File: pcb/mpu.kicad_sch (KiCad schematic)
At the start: 27 parts, among them J13 Conn_01x04, U2 STM32U585CIUxQ, Y1 ECS-160-8-36B2-CKM-TR, Y2 CM7V-T1A-32.768KHZ

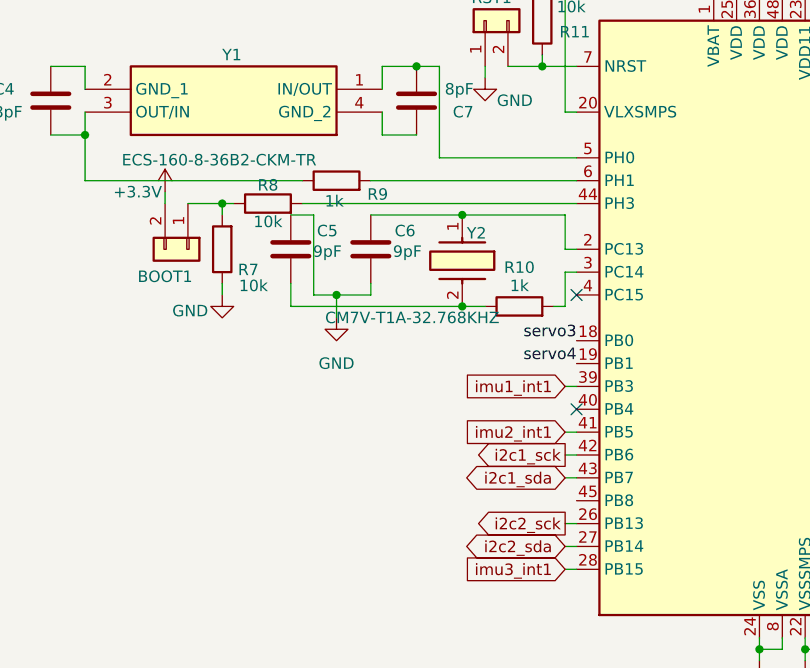
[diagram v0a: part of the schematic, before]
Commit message: rerouted oscillator stuff - still need to finish i2c routing, also started a platformio board definition
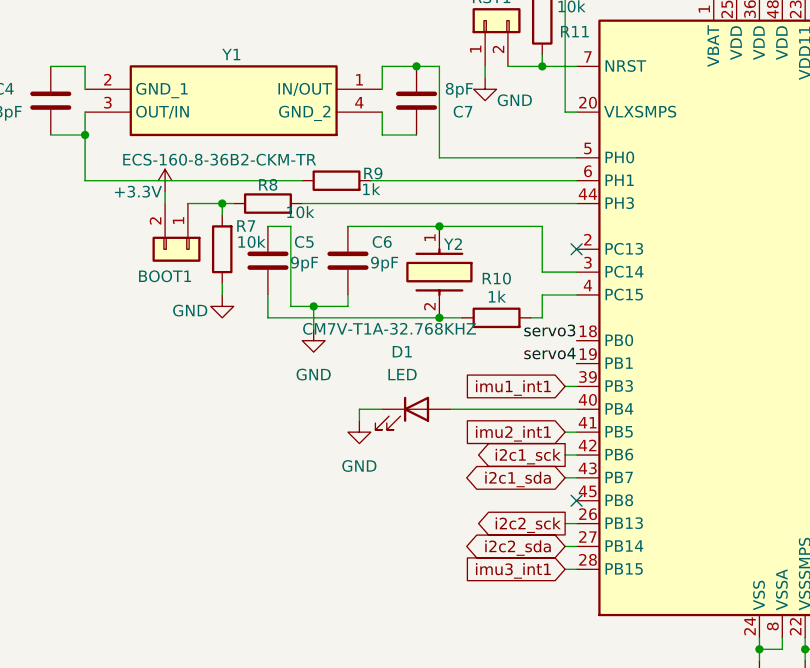
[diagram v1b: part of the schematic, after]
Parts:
- added D1: LED, symbol Device:LED
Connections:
- net GND: now also D1.1 (K)
- net at R10.2: now also U2.4 (PC15); no longer U2.3 (PC14)
- net at C6.1, Y2.1: now also U2.3 (PC14); no longer U2.2 (PC13)
- net at U2.40 (PB4): now also D1.2 (A)
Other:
- moved on the sheet: C5, C6, R10, Y2

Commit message: board def hopefully done, mpu test firmware written
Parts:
- J13: footprint Connector_PinHeader_2.54mm:PinHeader_1x04_P2.54mm_Vertical -> TerminalBlock:TerminalBlock_Xinya_XY308-2.54-4P_1x04_P2.54mm_Horizontal
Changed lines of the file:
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@@
 			)
 		)
-		(property "Footprint" "Connector_PinHeader_2.54mm:PinHeader_1x04_P2.54mm_Vertical"
+		(property "Footprint" "TerminalBlock:TerminalBlock_Xinya_XY308-2.54-4P_1x04_P2.54mm_Horizontal"
 			(at 222.25 76.2 0)
 			(effects

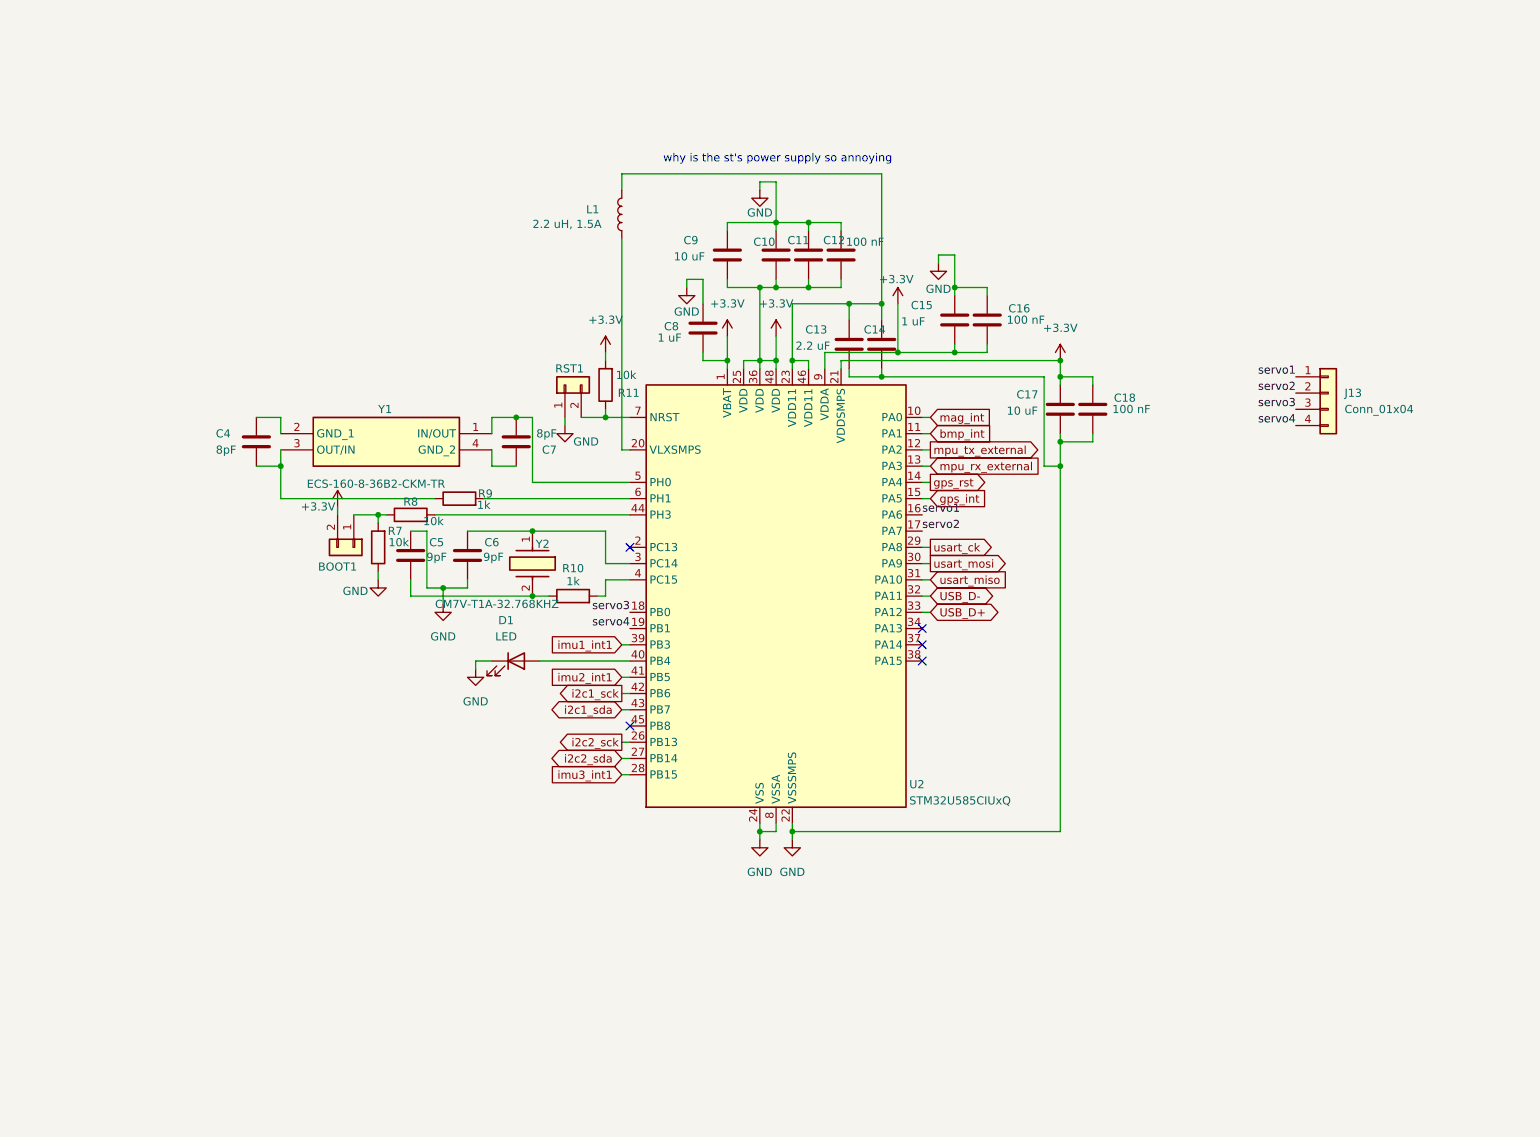
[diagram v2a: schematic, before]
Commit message: added models for some things, fixed micro sd impl and a bunch of other stuff - pcb currently probably ready for production
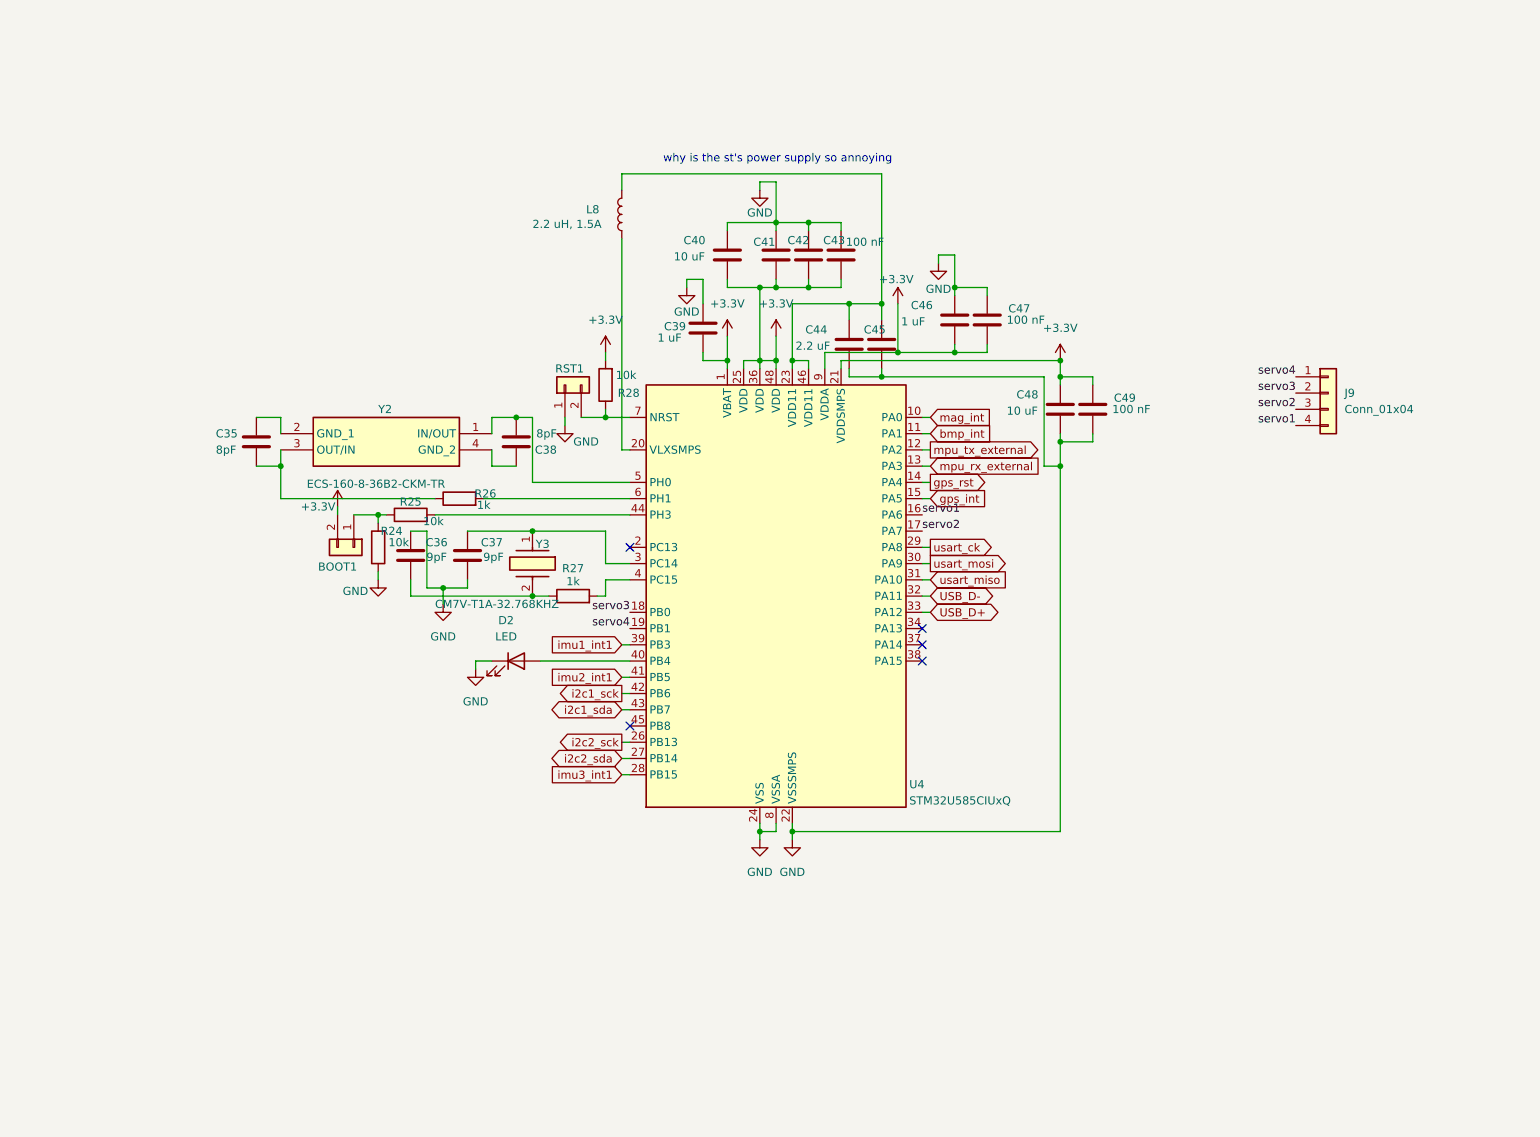
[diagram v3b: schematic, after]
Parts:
- renumbered C4 to C35, C5 to C36, C6 to C37, C7 to C38, C8 to C39, C9 to C40, C10 to C41, C11 to C42, C12 to C43, C13 to C44, C14 to C45, C15 to C46, C16 to C47, C17 to C48, C18 to C49, D1 to D2, J13 to J9, L1 to L8, R7 to R24, R8 to R25, R9 to R26, R10 to R27, R11 to R28, U2 to U4, Y1 to Y2, Y2 to Y3
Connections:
- net servo1: now also J9.4 (Pin_4); no longer J9.1 (Pin_1)
- net servo2: now also J9.3 (Pin_3); no longer J9.2 (Pin_2)
- net servo3: now also J9.2 (Pin_2); no longer J9.3 (Pin_3)
- net servo4: now also J9.1 (Pin_1); no longer J9.4 (Pin_4)

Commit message: started making bom - changed some stuff for compatibility with it
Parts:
- C39, C46: value 1 uF -> 1uF
- C40, C48: value 10 uF -> 10uF
- C41, C42, C43, C47, C49: value 100 nF -> 100nF
- C44, C45: value 2.2 uF -> 2.2uF
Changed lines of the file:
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@@
 			)
 		)
-		(property "Value" "1 uF"
+		(property "Value" "1uF"
 			(at 117.348 67.564 0)
 			(effects
@@
 			)
 		)
-		(property "Value" "2.2 uF"
+		(property "Value" "2.2uF"
 			(at 138.938 68.834 0)
 			(effects
@@
 			)
 		)
-		(property "Value" "100 nF"
+		(property "Value" "100nF"
 			(at 146.812 52.578 0)
 			(effects
@@
 			)
 		)
-		(property "Value" "10 uF"
+		(property "Value" "10uF"
 			(at 119.888 54.864 0)
 			(effects
@@
 			)
 		)
-		(property "Value" "100 nF"
+		(property "Value" "100nF"
 			(at 188.468 78.74 0)
 			(effects
@@
 			)
 		)
-		(property "Value" "100 nF"
+		(property "Value" "100nF"
 			(at 171.958 64.77 0)
 			(effects
@@
 			)
 		)
-		(property "Value" "100 nF"
+		(property "Value" "100nF"
 			(at 144.526 40.894 0)
 			(effects
@@
 			)
 		)
-		(property "Value" "1 uF"
+		(property "Value" "1uF"
 			(at 155.448 65.024 0)
 			(effects
@@
 			)
 		)
-		(property "Value" "2.2 uF"
+		(property "Value" "2.2uF"
 			(at 151.892 60.452 0)
 			(effects
@@
 			)
 		)
-		(property "Value" "100 nF"
+		(property "Value" "100nF"
 			(at 145.542 46.482 0)
 			(effects
@@
 			)
 		)
-		(property "Value" "10 uF"
+		(property "Value" "10uF"
 			(at 171.958 78.994 0)
 			(effects

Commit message: updated pcb from schematic changes, also added some length tuning because why not
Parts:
- renumbered J9 to SERVO1
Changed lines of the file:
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@@
 		(dnp no)
 		(fields_autoplaced yes)
-		(property "Reference" "J9"
+		(property "Reference" "SERVO1"
 			(at 224.79 76.1999 0)
 			(effects
@@
 			(project ""
 				(path "/d0cafa98-cc2a-4ab3-8dbc-f937bedf434b/94fda4c7-40dd-4c5d-acdd-b2f66ff666c2"
-					(reference "J9")
+					(reference "SERVO1")
 					(unit 1)
 				)

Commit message: mainly worked on bom (still just on google sheets), but while doing so fixed some issues and redid some component selection
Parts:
- SERVO1: footprint TerminalBlock:TerminalBlock_Xinya_XY308-2.54-4P_1x04_P2.54mm_Horizontal -> footprints:TBC05041GG
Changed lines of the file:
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@@
 			)
 		)
-		(property "Footprint" "TerminalBlock:TerminalBlock_Xinya_XY308-2.54-4P_1x04_P2.54mm_Horizontal"
+		(property "Footprint" "footprints:TBC05041GG"
 			(at 222.25 76.2 0)
 			(effects

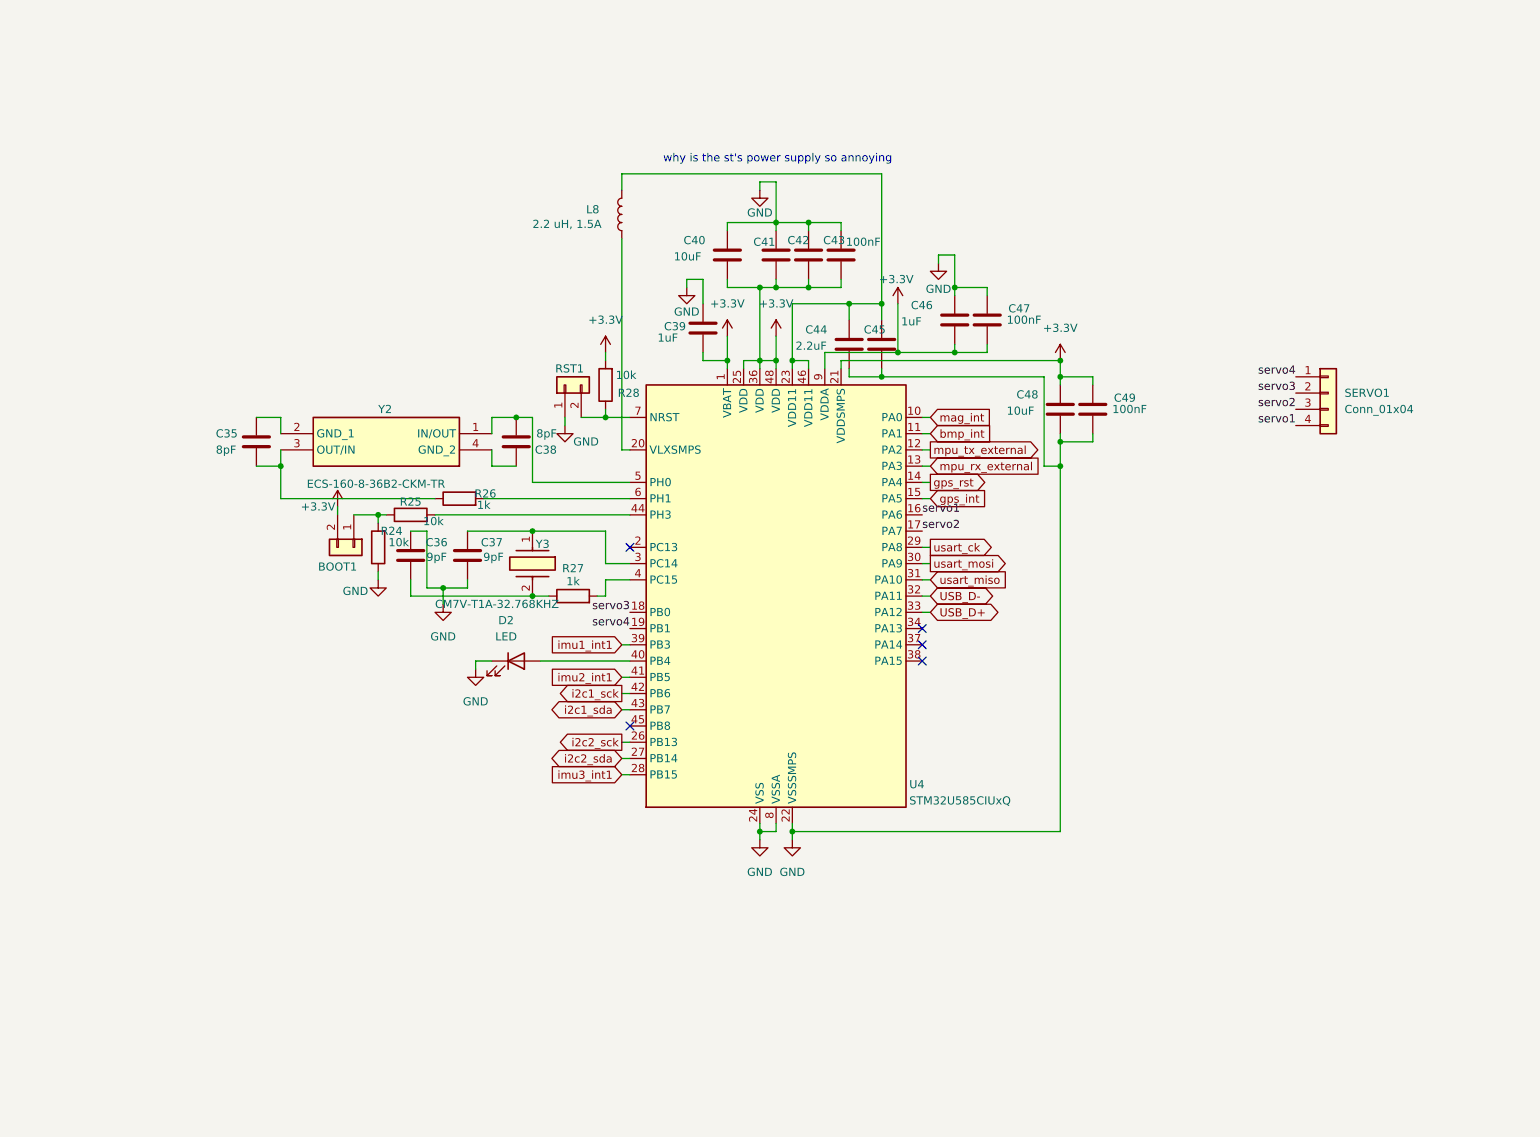
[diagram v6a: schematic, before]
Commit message: reorganized schematic, started to add a readme (not really though), also pcb updated
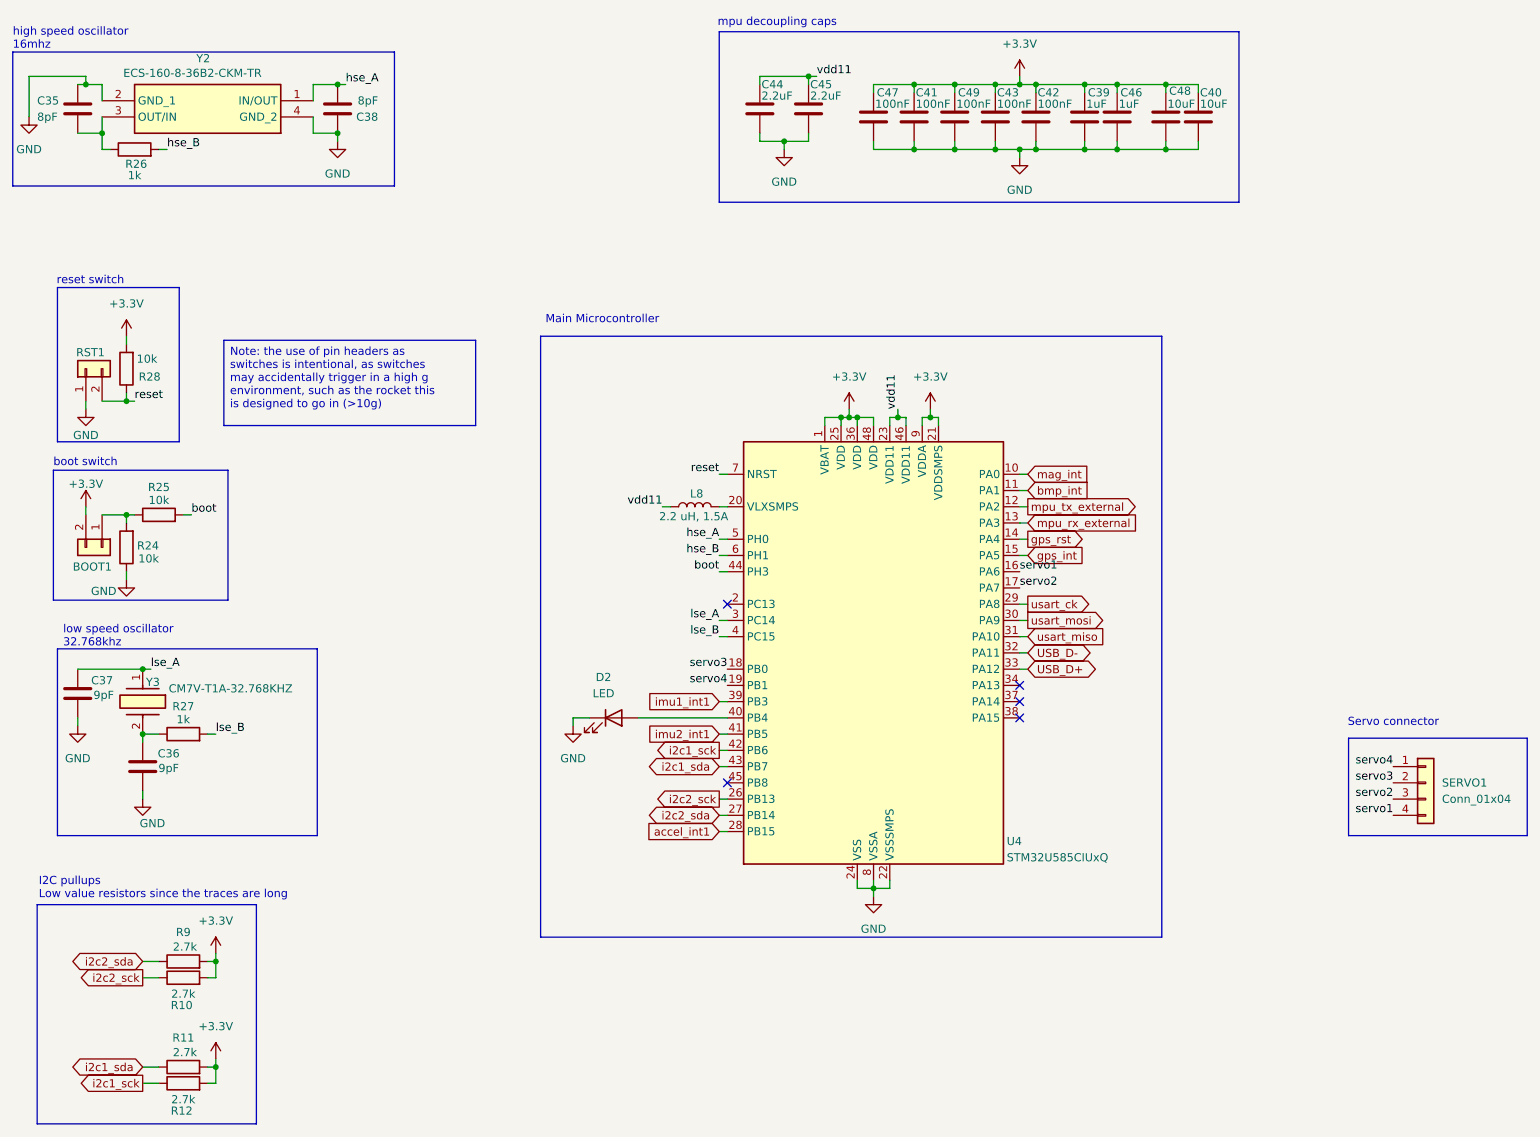
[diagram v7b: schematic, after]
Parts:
- added R10, R11, R12, R9: 2.7k, Resistor_SMD:R_0402_1005Metric, symbol Device:R
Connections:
- net +3.3V: now also C39.1, C40.1, C41.1, C42.1, C43.1, C46.1, C47.1, R10.2, R11.2, R12.2, R9.2; no longer C39.2, C40.2, C41.2, C42.2, C43.2, C46.2, C47.2
- net GND: now also C35.2, C36.2, C38.2, C39.2, C40.2, C41.2, C42.2, C43.2, C46.2, C47.2, Y2.2 (GND_1), Y2.4 (GND_2); no longer C36.1, C39.1, C40.1, C41.1, C42.1, C43.1, C46.1, C47.1
- net i2c1_sck: now also R12.1
- net i2c1_sda: now also R11.1
- net i2c2_sck: now also R10.1
- net i2c2_sda: now also R9.1
- net vdd11: now reaches C44.1, C45.1, U4.23 (VDD11), U4.46 (VDD11)
- net vdd11: now also L8.1; no longer L8.2
- net hse_B: now reaches R26.2, U4.6 (PH1)
- net boot: now reaches R25.2, U4.44 (PH3)
- net reset: now reaches R28.1, RST1.2 (Pin_2), U4.7 (NRST)
- net at U4.20 (VLXSMPS): now also L8.2; no longer L8.1
- net at R27.1, Y3.2: now also C36.1; no longer C36.2
- net lse_B: now reaches R27.2, U4.4 (PC15)
- net hse_A: now reaches C38.1, U4.5 (PH0), Y2.1 (IN/OUT)
- net lse_A: now reaches C37.1, U4.3 (PC14), Y3.1
- net imu3_int1 renamed accel_int1
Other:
- note added: "I2C pullups Low value resistors since the traces are long"
- note added: "Main Microcontroller"
- note added: "Servo connector"
- note added: "boot switch"
- note added: "high speed oscillator 16mhz"
- note added: "low speed oscillator 32.768khz"
- note added: "mpu decoupling caps"
- note added: "reset switch"
- note removed: "why is the st's power supply so annoying"
- moved on the sheet: BOOT1, C35, C36, C37, C38, C39, C40, C41, C42, C43, C44, C45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
